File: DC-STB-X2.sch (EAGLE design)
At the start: 1 part

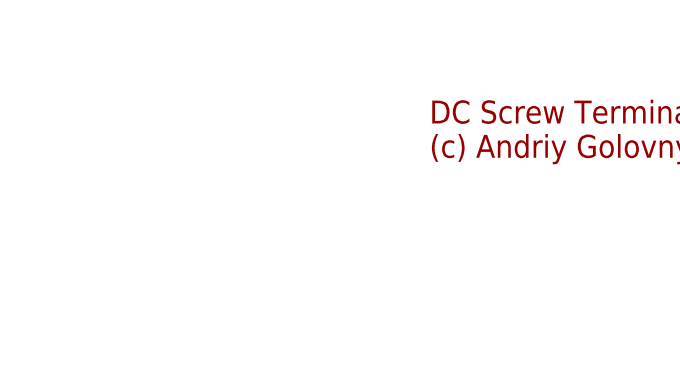
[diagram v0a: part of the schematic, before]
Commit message: Added logos to all boards. Generated CAM files.
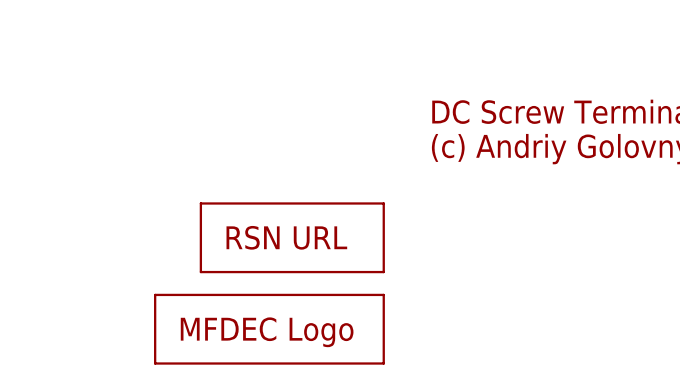
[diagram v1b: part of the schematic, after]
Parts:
- added LOGO1: MFDECLOGO_L_10MM, _my_logos:MFDECLOGO_L_10MM
- added LOGO2: RSNURL_QR_10MM, _my_logos:RSNURL_QR_10MM
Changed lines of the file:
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@@
 <layer number="97" name="Info" color="7" fill="1" visible="yes" active="yes"/>
 <layer number="98" name="Guide" color="6" fill="1" visible="yes" active="yes"/>
+<layer number="200" name="200bmp" color="1" fill="10" visible="yes" active="yes"/>
 </layers>
 <schematic xreflabel="%F%N/%S.%C%R" xrefpart="/%S.%C%R">
@@
 <part name="FRAME1" library="frames" library_urn="urn:adsk.eagle:library:229" deviceset="DINA4_L" device=""/>
 <part name="U$1" library="KF8500-Terminals" deviceset="KF8500-8.5-2P" device=""/>
+<part name="LOGO1" library="_my_logos" deviceset="MFDECLOGO" device="_L_10MM"/>
+<part name="LOGO2" library="_my_logos" deviceset="RSNURL" device="_QR_10MM"/>
 </parts>
 <sheets>
@@
 <instance part="U$1" gate="G$1" x="132.08" y="116.84" smashed="yes"/>
 <instance part="U$1" gate="G$2" x="132.08" y="111.76" smashed="yes"/>
+<instance part="LOGO1" gate="G$1" x="134.62" y="2.54" smashed="yes"/>
+<instance part="LOGO2" gate="G$1" x="139.7" y="12.7" smashed="yes"/>
 </instances>
 <busses>
